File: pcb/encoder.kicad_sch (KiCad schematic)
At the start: 22 parts, among them J1 Conn_01x04_Pin, U4 74AUP1G373, U5 74AUP1G373, U6 74LVC1G08, U7 74LVC1G08

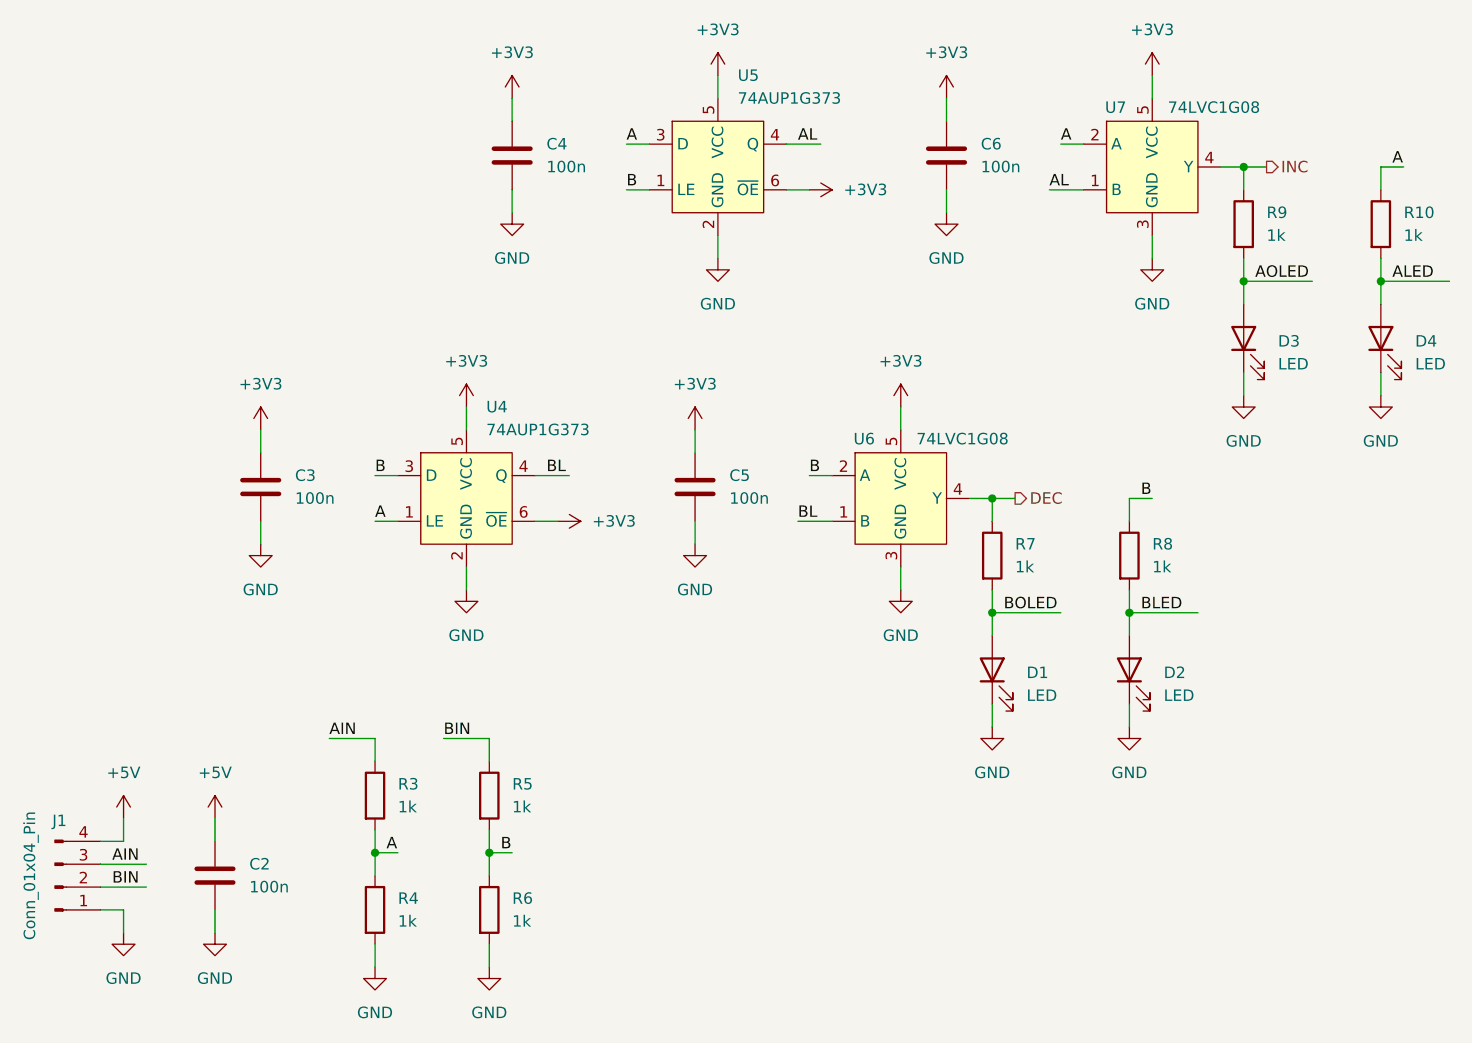
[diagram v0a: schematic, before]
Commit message: Remove sensor hub
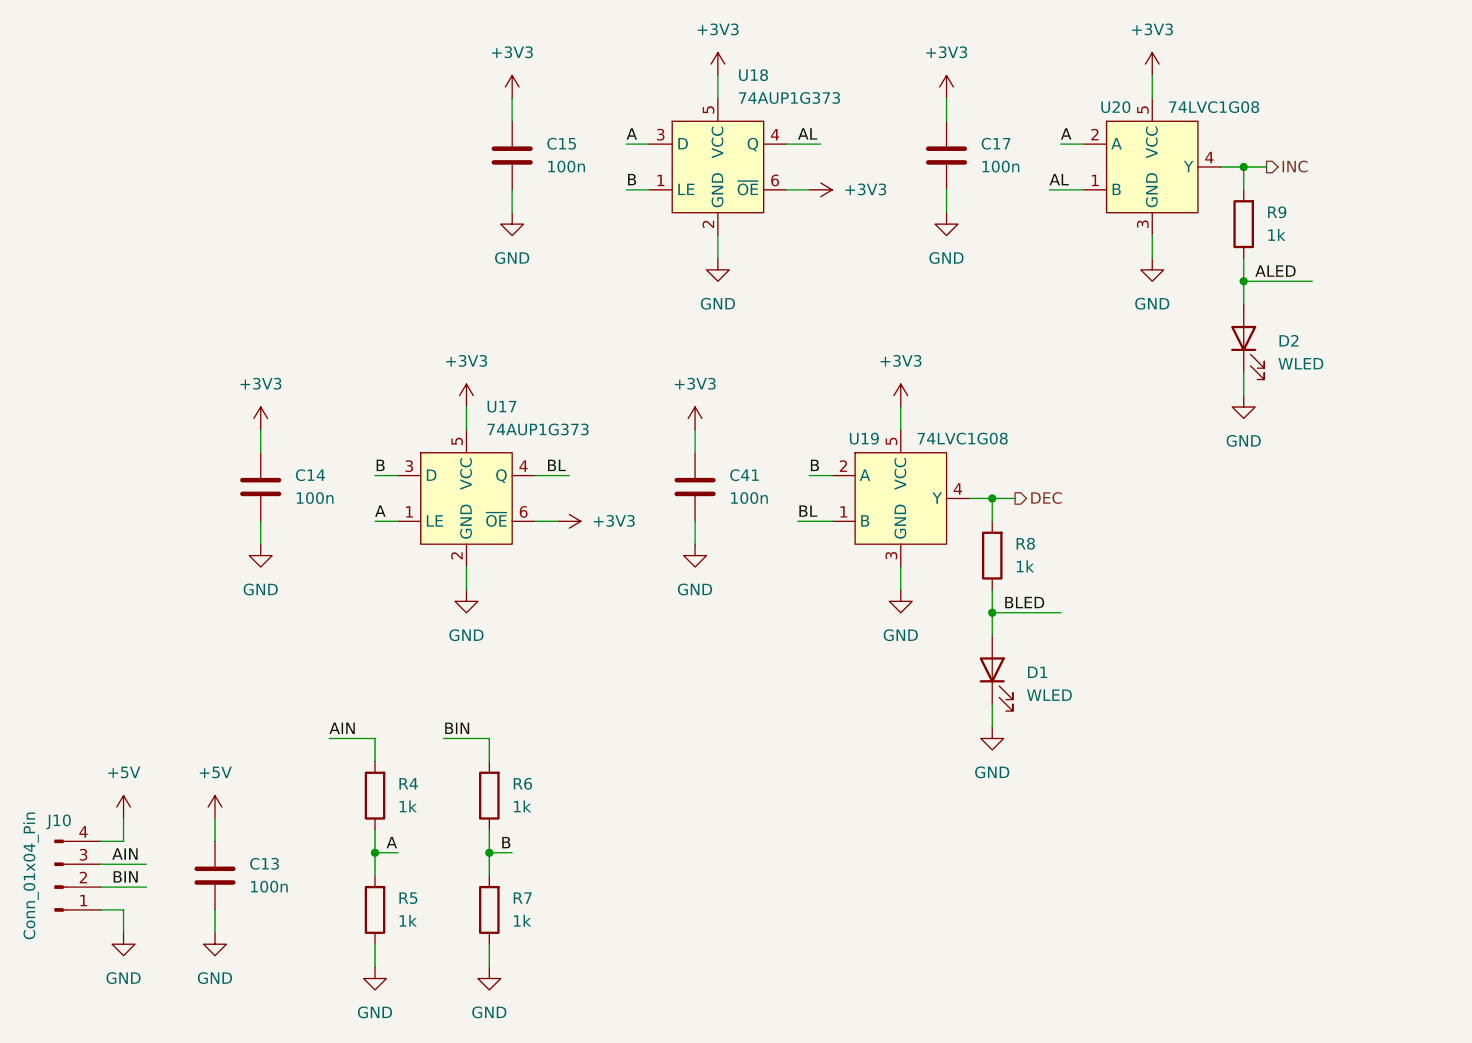
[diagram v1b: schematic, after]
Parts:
- removed C2, C3, C4, C6: 100n, symbol Device:C
- removed D3, D4: LED, symbol Device:LED
- removed R10, R3: 1k, symbol Device:R
- added C13, C14, C15, C17: 100n, Capacitor_SMD:C_0402_1005Metric, symbol Device:C
- C41: renamed from C5; footprint (none) -> Capacitor_SMD:C_0402_1005Metric; LCSC (none) -> C1525
- D1, D2: value LED -> WLED; footprint (none) -> LED_SMD:LED_0603_1608Metric; LCSC (none) -> C2290
- J10: renamed from J1; footprint (none) -> Connector_PinHeader_2.54mm:PinHeader_1x04_P2.54mm_Vertical; LCSC (none) -> C6332197
- R4, R5, R6, R7, R8, R9: footprint (none) -> Resistor_SMD:R_0402_1005Metric; LCSC (none) -> C11702
- U17: renamed from U4; LCSC (none) -> C458800
- U18: renamed from U5; LCSC (none) -> C458800
- U19: renamed from U6; LCSC (none) -> C12512
- U20: renamed from U7; LCSC (none) -> C12512
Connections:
- net AOLED is gone; now on net INC: R9.2
- net +3V3: now also C14.1, C15.1, C17.1
- net +5V: now also C13.1
- net A: now also R5.2
- net AIN: now also R4.2
- net ALED: now also D2.2 (A), R9.1
- net B: now also R7.2; no longer R5.2, R8.1
- net BIN: now also R6.2; no longer R5.1
- net BLED: now also D1.2 (A), R8.1; no longer D2.2 (A), R8.2
- net DEC: now also R8.2; no longer R7.1
- net GND: now also R5.1, R7.1, C13.2, C14.2, C15.2, C17.2; no longer R4.2, R6.2
- net INC: no longer R9.1
- removed net BOLED: D1.2 (A), R7.2

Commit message: Finish schematic
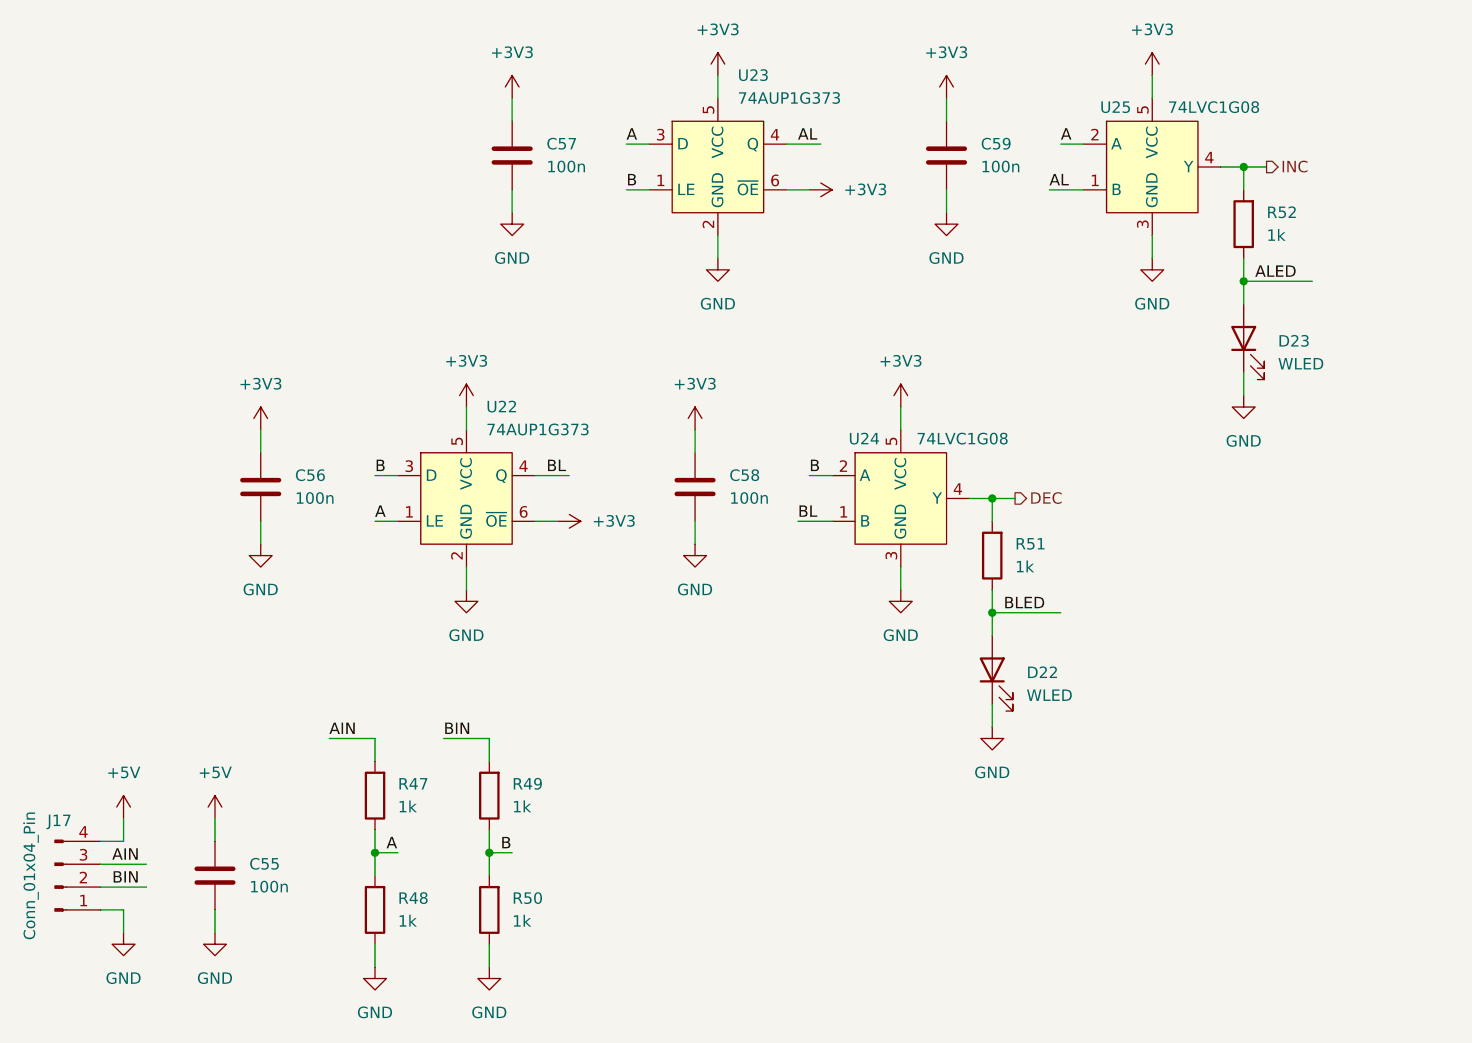
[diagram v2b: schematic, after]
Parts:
- renumbered C13 to C55, C14 to C56, C15 to C57, C41 to C58, C17 to C59, D1 to D22, D2 to D23, J10 to J17, R4 to R47, R5 to R48, R6 to R49, R7 to R50, R8 to R51, R9 to R52, U17 to U22, U18 to U23, U19 to U24, U20 to U25

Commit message: Save progress
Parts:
- removed C56, C57, C58, C59: 100n, Capacitor_SMD:C_0402_1005Metric, symbol Device:C
- removed D22, D23: WLED, LED_SMD:LED_0603_1608Metric, symbol Device:LED
- removed R51, R52: 1k, Resistor_SMD:R_0402_1005Metric, symbol Device:R
- removed U22, U23: 74AUP1G373, Package_TO_SOT_SMD:SOT-363_SC-70-6, symbol Symbols:74AUP1G373
- removed U24, U25: 74LVC1G08, Package_TO_SOT_SMD:SOT-353_SC-70-5, symbol Symbols:74LVC1G08
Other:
- moved on the sheet: C55, J17, R47, R48, R49, R50

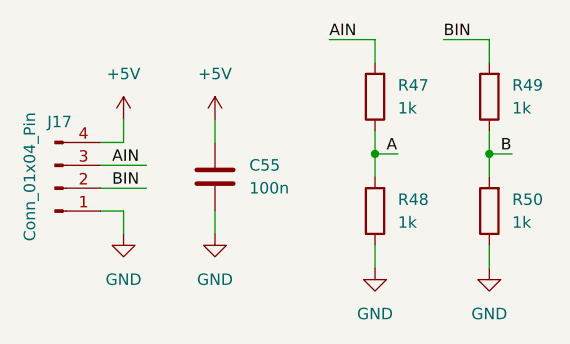
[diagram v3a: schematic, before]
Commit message: Finish first draft schematic
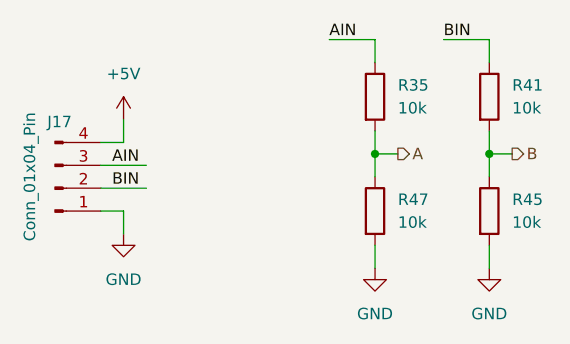
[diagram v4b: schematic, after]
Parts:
- removed C55: 100n, Capacitor_SMD:C_0402_1005Metric, symbol Device:C
- removed R48, R49, R50: 1k, Resistor_SMD:R_0402_1005Metric, symbol Device:R
- added R35, R41, R45: 10k, Resistor_SMD:R_0402_1005Metric, symbol Device:R
- R47: value 1k -> 10k; LCSC C11702 -> C25744
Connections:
- net A: now also R35.2
- net AIN: now also R35.1; no longer R47.2
- net B: now also R41.2, R45.1
- net BIN: now also R41.1
- net GND: now also R47.2, R45.2

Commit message: Save progress
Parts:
- J17: now not fitted
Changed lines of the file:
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@@
 		(in_bom yes)
 		(on_board yes)
-		(dnp no)
+		(dnp yes)
 		(property "Reference" "J17"
-			(at 56.388 51.054 0)
+			(at 56.896 49.784 0)
 			(effects
 				(font

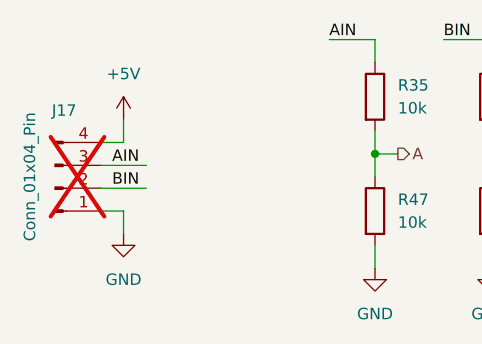
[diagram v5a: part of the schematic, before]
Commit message: Finish schematic
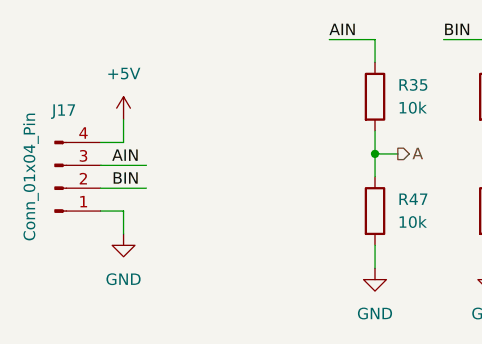
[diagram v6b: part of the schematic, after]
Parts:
- J17: now fitted
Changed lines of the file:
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@@
 		(in_bom yes)
 		(on_board yes)
-		(dnp yes)
+		(dnp no)
 		(property "Reference" "J17"
 			(at 56.896 49.784 0)

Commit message: Add power switch
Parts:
- J17: now not fitted
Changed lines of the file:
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@@
 		(in_bom yes)
 		(on_board yes)
-		(dnp no)
+		(dnp yes)
 		(property "Reference" "J17"
 			(at 56.896 49.784 0)

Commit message: Finish for revision 2 production
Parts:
- R35, R41, R45, R47: value 10k -> 7k5; LCSC C25744 -> C25918
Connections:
- net +5V: now also J17.2 (Pin_2); no longer J17.4 (Pin_4)
- net BIN: now also J17.4 (Pin_4); no longer J17.2 (Pin_2)
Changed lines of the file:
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@@
+	(wire
+		(pts
+			(xy 63.5 50.8) (xy 63.5 58.42)
+		)
+		(stroke
+			(width 0)
+			(type default)
+		)
+	)
 	(wire
 		(pts
@@
 	(wire
 		(pts
+			(xy 60.96 53.34) (xy 69.85 53.34)
+		)
+		(stroke
+			(width 0)
+			(type default)
+		)
+	)
+	(wire
+		(pts
 			(xy 104.14 54.61) (xy 104.14 57.15)
 		)
@@
 	(wire
 		(pts
-			(xy 63.5 53.34) (xy 60.96 53.34)
+			(xy 63.5 58.42) (xy 60.96 58.42)
 		)
 		(stroke
@@
 	(wire
 		(pts
-			(xy 63.5 50.8) (xy 63.5 53.34)
-		)
-		(stroke
-			(width 0)
-			(type default)
-		)
-	)
-	(wire
-		(pts
 			(xy 104.14 64.77) (xy 104.14 67.31)
 		)
@@
 	(wire
 		(pts
-			(xy 60.96 55.88) (xy 66.04 55.88)
-		)
-		(stroke
-			(width 0)
-			(type default)
-		)
-	)
-	(wire
-		(pts
 			(xy 91.44 54.61) (xy 93.98 54.61)
 		)
@@
 	(wire
 		(pts
-			(xy 60.96 58.42) (xy 66.04 58.42)
+			(xy 60.96 55.88) (xy 69.85 55.88)
 		)
 		(stroke
@@
 		)
 	)
-	(label "BIN"
-		(at 62.23 58.42 0)
+	(label "AIN"
+		(at 66.04 55.88 0)
 		(fields_autoplaced yes)
 		(effects
@@
 		)
 	)
-	(label "AIN"
-		(at 62.23 55.88 0)
+	(label "BIN"
+		(at 66.04 53.34 0)
 		(fields_autoplaced yes)
 		(effects
@@
 			)
 		)
-		(property "Value" "10k"
+		(property "Value" "7k5"
 			(at 93.98 62.2299 0)
 			(effects
@@
 			)
 		)
-		(property "LCSC" "C25744"
+		(property "LCSC" "C25918"
 			(at 91.44 60.96 0)
 			(effects
@@
 			)
 		)
-		(property "Value" "10k"
+		(property "Value" "7k5"
 			(at 106.68 62.2299 0)
 			(effects
@@
 			)
 		)
-		(property "LCSC" "C25744"
+		(property "LCSC" "C25918"
 			(at 104.14 60.96 0)
 			(effects
@@
 			)
 		)
-		(property "Value" "10k"
+		(property "Value" "7k5"
 			(at 106.68 49.5299 0)
 			(effects
@@
 			)
 		)
-		(property "LCSC" "C25744"
+		(property "LCSC" "C25918"
 			(at 104.14 48.26 0)
 			(effects
@@
 			)
 		)
-		(property "Value" "10k"
+		(property "Value" "7k5"
 			(at 93.98 49.5299 0)
 			(effects
@@
 			)
 		)
-		(property "LCSC" "C25744"
+		(property "LCSC" "C25918"
 			(at 91.44 48.26 0)
 			(effects
